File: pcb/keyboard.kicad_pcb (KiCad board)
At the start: 2 copper layers, 331.1 x 102 mm, 140 parts, among them J1 USB_C_Receptacle_USB2.0, Q1 BC858, SW1 SW_Push, SW10 SW_Push, SW11 SW_Push, SW12 SW_Push, SW13 SW_Push, SW14 SW_Push, SW15 SW_Push, SW16 SW_Push, SW17 SW_Push, SW18 SW_Push, SW19 SW_Push, SW2 SW_Push, SW20 SW_Push, SW21 SW_Push, SW22 SW_Push, SW23 SW_Push, SW24 SW_Push, SW25 SW_Push, SW26 SW_Push, SW27 SW_Push, SW28 SW_Push, SW29 SW_Push, SW3 SW_Push, SW30 SW_Push, SW31 SW_Push, SW32 SW_Push, SW33 SW_Push, SW34 SW_Push, SW35 SW_Push, SW36 SW_Push, SW37 SW_Push, SW38 SW_Push, SW39 SW_Push, SW4 SW_Push, SW40 SW_Push, SW41 SW_Push, SW42 SW_Push, SW43 SW_Push, SW44 SW_Push, SW45 SW_Push, SW46 SW_Push, SW47 SW_Push, SW48 SW_Push, SW49 SW_Push, SW5 SW_Push, SW50 SW_Push, SW6 SW_Push, SW7 SW_Push, SW8 SW_Push, SW9 SW_Push, U1 NCP1117-3.3_SOT223, U2 USBLC6-2SC6, U3 W25Q128JVS, U4 RP2040, Y1 ABM8-272_T3

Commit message: More routing yippieeeee
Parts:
- removed the C16 at (206.2, 156.2)
- moved TP2 2.00 mm to (214.0, 164.2)
- moved TP1 1.75 mm to (210.8, 164.2)
- moved D18 1.27 mm to (133.5, 170.5), turned to -102 degrees
- moved D26 0.79 mm to (176.8, 183.0), turned to -117 degrees
- moved D14 0.25 mm to (115.2, 165.2), turned to -102 degrees
- renumbered C17 to C16
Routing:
- net /MCU/row0: track 136.2 -> 417.1 mm
- net /MCU/row1: track 120.3 -> 387.3 mm
- net /MCU/row2: track 120.3 -> 366.8 mm
- net /MCU/row3: track 68.9 -> 221.7 mm
- net +3V3: track 102.3 -> 141.7 mm, vias 5 -> 7
- net /MCU/col7: track 53.7 -> 82.2 mm, vias 1 -> 2
- net /MCU/col13: track 41.6 -> 51.8 mm, vias 0 -> 1
- net /MCU/col12: track 41.6 -> 51.3 mm, vias 0 -> 1
- net /MCU/col11: track 41.8 -> 51.0 mm, vias 0 -> 1
- net /MCU/col10: track 61.9 -> 70.7 mm, vias 0 -> 1
- net Net-(D4-A): track 0.00 -> 8.73 mm
- net Net-(D7-A): track 0.00 -> 8.62 mm
- net Net-(D10-A): track 0.00 -> 8.52 mm
- net /MCU/col9: track 61.9 -> 70.4 mm, vias 0 -> 1
- net /MCU/col8: track 62.1 -> 70.4 mm, vias 0 -> 1
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
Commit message: Preliminary routing done
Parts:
- TP1, TP2: moved to B.Cu
- moved R1 43.8 mm to (227.0, 127.8), turned to 180 degrees
- moved R2 40.8 mm to (227.0, 126.2), turned to 0 degrees
- moved R3 37.8 mm to (227.0, 124.8), turned to 180 degrees
- moved D1 33.8 mm to (227.0, 122.8), turned to 180 degrees
- moved TP1 5.46 mm to (205.5, 162.8), turned to 180 degrees
- moved TP2 4.98 mm to (209.2, 162.8), turned to 180 degrees
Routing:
- net /MCU/col0: track 40.4 -> 239.0 mm, vias 0 -> 1
- net /MCU/col1: track 40.4 -> 218.5 mm, vias 0 -> 1
- net /MCU/col13: track 51.8 -> 228.1 mm
- net /MCU/col12: track 51.3 -> 208.4 mm
- net /MCU/col2: track 40.4 -> 196.8 mm, vias 0 -> 1
- net /MCU/col11: track 51.0 -> 187.4 mm
- net /MCU/col3: track 60.7 -> 196.7 mm, vias 0 -> 1
- net /MCU/col4: track 60.7 -> 176.6 mm, vias 0 -> 1
- net /MCU/col10: track 70.7 -> 185.4 mm
- net /MCU/col9: track 70.4 -> 168.3 mm
- net /MCU/col5: track 60.7 -> 158.2 mm, vias 0 -> 1
- net /MCU/col8: track 70.4 -> 148.2 mm
- net /MCU/col6: track 70.1 -> 137.9 mm, vias 0 -> 1
- net /MCU/col7: track 82.2 -> 121.0 mm
- net /MCU/row3: track 221.7 -> 260.2 mm, vias 0 -> 2
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- added copper zone on B.Cu, net GND
- added copper zone on F.Cu, net GND

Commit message: PCB updates, cad updates
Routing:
- net VBUS: track 29.8 -> 33.8 mm
- net GND: track 5.91 -> 7.47 mm
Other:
- board text added: "3V3"
- board text added: "SWCLK"
- board text added: "SWDIO"

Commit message: Ready to produce test production files before updating some components
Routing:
- net +3V3: track 147.4 -> 148.9 mm
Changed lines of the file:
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@@
   (segment (start 217.75 145) (end 216.5375 146.2125) (width 0.25) (layer "B.Cu") (net 3))
   (segment (start 209.1375 144) (end 207.75 142.6125) (width 0.25) (layer "B.Cu") (net 3))
+  (segment (start 206.25 142.6125) (end 207.75 142.6125) (width 0.25) (layer "B.Cu") (net 3))
   (segment (start 219.8625 132.1375) (end 218 134) (width 0.25) (layer "B.Cu") (net 3))
   (segment (start 208.075 146.2125) (end 206.3625 144.5) (width 0.25) (layer "B.Cu") (net 3))

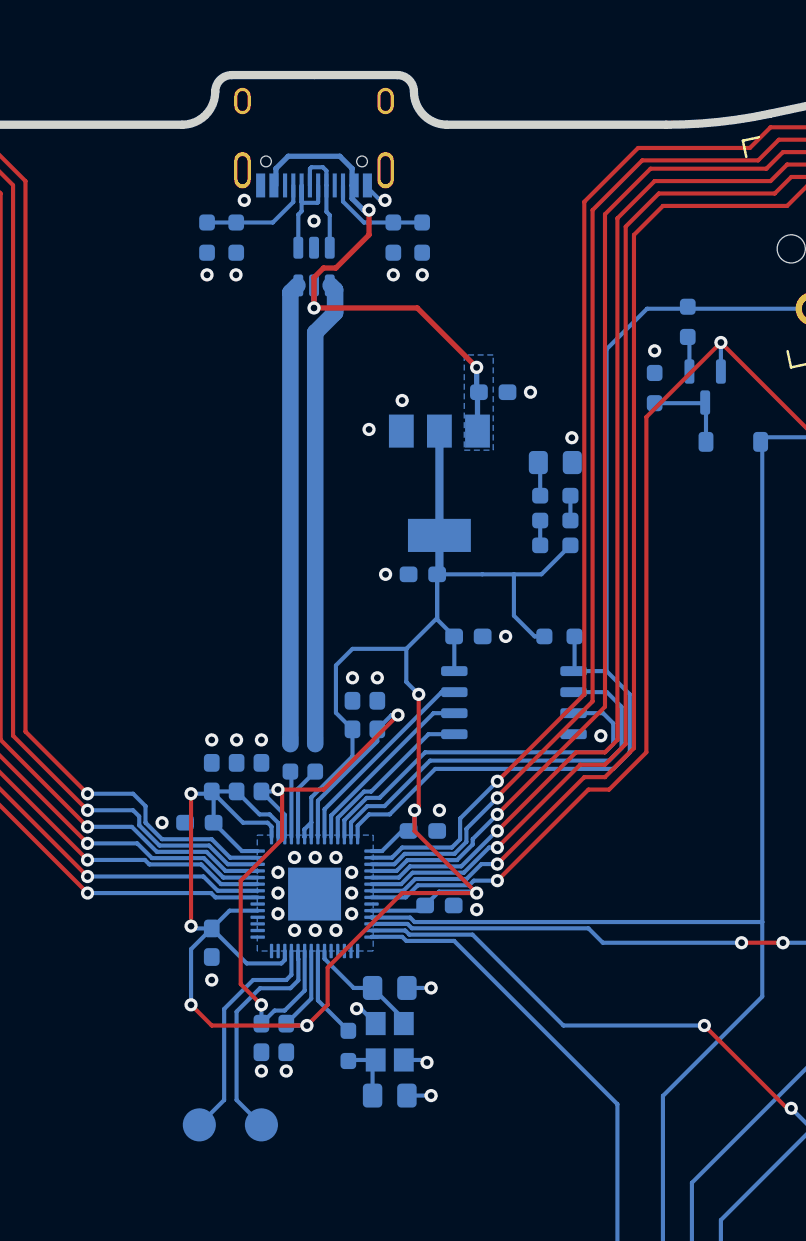
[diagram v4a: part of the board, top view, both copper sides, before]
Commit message: Rerouted a lot of stuff
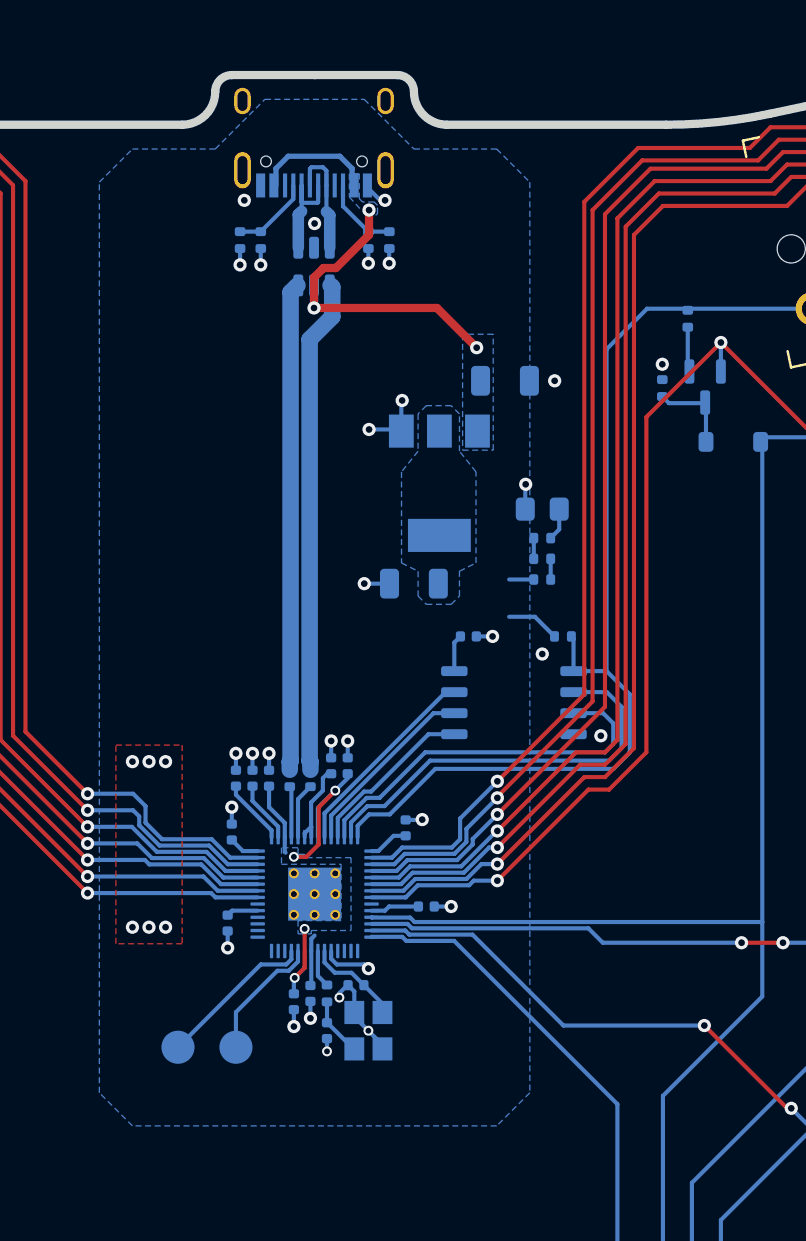
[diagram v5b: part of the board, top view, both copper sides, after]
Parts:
- added ?: , , F.Cu at (213.7, 148.8)
- added ?: , , F.Cu at (212.5, 148.8)
- added ?: , , F.Cu at (213.7, 150.1)
- added ?: , , F.Cu at (212.5, 147.6)
- added ?: , , F.Cu at (211.2, 147.6)
- added ?: , , F.Cu at (211.2, 148.8)
- added ?: , , F.Cu at (213.7, 147.6)
- added ?: , , F.Cu at (212.5, 150.1)
- added ?: , , F.Cu at (211.2, 150.1)
- C1: footprint Capacitor_SMD:C_0603_1608Metric_Pad1.08x0.95mm_HandSolder -> Capacitor_SMD:C_1206_3216Metric
- C10, C11, C12, C13, C14, C15, C5, C6, C7, C8, C9: footprint Capacitor_SMD:C_0603_1608Metric_Pad1.08x0.95mm_HandSolder -> Capacitor_SMD:C_0402_1005Metric
- C16: value 100n -> 10u; footprint Capacitor_SMD:C_0603_1608Metric_Pad1.08x0.95mm_HandSolder -> Capacitor_SMD:C_1206_3216Metric
- C2: value 10u -> 100n; footprint Capacitor_SMD:C_0603_1608Metric_Pad1.08x0.95mm_HandSolder -> Capacitor_SMD:C_0402_1005Metric
- C3, C4: footprint Capacitor_SMD:C_0805_2012Metric_Pad1.18x1.45mm_HandSolder -> Capacitor_SMD:C_0402_1005Metric
- R1, R10, R11, R12, R13, R2, R3, R4, R5, R6, R7, R8, R9: footprint Resistor_SMD:R_0603_1608Metric_Pad0.98x0.95mm_HandSolder -> Resistor_SMD:R_0402_1005Metric
- moved C16 14.9 mm to (218.5, 130.1), turned to 180 degrees
- moved C2 12.4 mm to (214.5, 141.1), turned to 90 degrees
- moved R7 9.75 mm to (209.2, 109.3)
- moved R4 9.75 mm to (215.7, 109.3)
- moved R6 9.26 mm to (208.0, 109.3)
- moved R5 9.25 mm to (217.0, 109.3)
- moved C7 7.02 mm to (218.0, 144.8)
- moved C4 5.45 mm to (213.2, 157.1), turned to -90 degrees
- moved TP2 4.93 mm to (207.7, 158.1)
- moved TP1 4.86 mm to (204.2, 158.1)
- moved R11 3.42 mm to (213.2, 154.8)
- moved C10 3.32 mm to (213.5, 141.1)
- moved C15 3.06 mm to (212.2, 154.8)
- moved C6 2.94 mm to (211.2, 155.3)
- moved D1 2.92 mm to (226.2, 125.6), turned to 0 degrees
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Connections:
- C2 pad 1: +3V3 -> +1V1
- C4 pad 1: GND -> Net-(C4-Pad1)
- C4 pad 2: Net-(C4-Pad2) -> GND
- C7 pad 1: +1V1 -> +3V3
- R11 pad 1: Net-(C4-Pad2) -> Net-(C4-Pad1)
- R4 pad 1: /connectors/CC1 -> /connectors/CC2
- R5 pad 1: /connectors/CC1 -> /connectors/CC2
- R6 pad 1: /connectors/CC2 -> /connectors/CC1
- R7 pad 1: /connectors/CC2 -> /connectors/CC1
- Y1 pad 3: Net-(C4-Pad2) -> Net-(C4-Pad1)
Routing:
- net +3V3: track 148.9 -> 32.2 mm, vias 7 -> 6
- net GND: track 7.47 -> 33.8 mm, vias 42 -> 31
- net +1V1: track 44.7 -> 20.5 mm, vias 3 -> 4
- net VBUS: track 33.8 -> 27.2 mm
- net /MCU/SWCLK: track 13.8 -> 7.77 mm
- net /MCU/SWDIO: track 14.0 -> 9.55 mm
- net Net-(C4-Pad2): track 3.90 -> 0.00 mm
- net Net-(C4-Pad1): track 0.00 -> 3.56 mm
- net /MCU/XOUT: track 5.58 -> 2.28 mm
- net /connectors/CC1: track 6.72 -> 4.85 mm
- net /connectors/CC2: track 6.28 -> 4.69 mm
- net /MCU/USB_D+: track 28.3 -> 29.9 mm
- net /MCU/USB_D-: track 27.9 -> 29.4 mm
- net /MCU/XIN: track 7.03 -> 5.75 mm
- net Net-(U4-USB_DP): track 4.39 -> 3.36 mm
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- added copper zone on B.Cu, net +1V1
- added copper zone on B.Cu, net +3V3
- added copper zone on F.Cu, net +3V3

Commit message: Further updates to routing
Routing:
- net /MCU/row2: track 398.4 -> 352.2 mm, vias 2 -> 3
- net /MCU/row0: track 440.8 -> 395.1 mm, vias 0 -> 3
- net /MCU/row1: track 417.9 -> 374.6 mm, vias 2 -> 3
- net /MCU/row3: track 260.2 -> 254.4 mm, vias 2 -> 0
- net GND: track 33.8 -> 35.7 mm

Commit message: PCB design complete
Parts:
- added G***: LOGO, local-library:monkei_but_smaller, B.Cu at (200.8, 125.6)
- added TP3: TestPoint, TestPoint:TestPoint_Pad_D2.0mm, B.Cu at (200.7, 158.1)
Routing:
- net VBUS: track 27.2 -> 29.3 mm
- net GND: track 35.7 -> 37.7 mm, vias 31 -> 36
- net +3V3: track 32.2 -> 30.7 mm
- net /MCU/col13: track 228.1 -> 227.4 mm
- net /MCU/col0: track 239.0 -> 238.4 mm
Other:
- board text added: "CLK"
- board text added: "Designed by Jack Bradley"
- board text added: "GND"
- board text added: "IO"
- board text added: "JLCJLCJLCJLC"
- board text added: "Just In Case"
- board text added: "Thingamaboard"
- board text added: "v2.0"
- board text removed: "SWCLK"
- board text removed: "SWDIO"
